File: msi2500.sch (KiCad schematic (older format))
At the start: 12 parts

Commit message: msi2500 full pcb design
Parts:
- removed U?: msi2500, symbol msi2500
- added C43: 10uF, symbol C
- added J10: GPIO2, Connectors:Pin_d0.7mm_L6.5mm_W1.8mm_FlatFork, symbol Conn_01x01
- added J11: GPIO3, Connectors:Pin_d0.7mm_L6.5mm_W1.8mm_FlatFork, symbol Conn_01x01
- added J7: VCC_GPIO, Connectors:Pin_d0.7mm_L6.5mm_W1.8mm_FlatFork, symbol Conn_01x01
- added J8: GPIO0, Connectors:Pin_d0.7mm_L6.5mm_W1.8mm_FlatFork, symbol Conn_01x01
- added J9: GPIO1, Connectors:Pin_d0.7mm_L6.5mm_W1.8mm_FlatFork, symbol Conn_01x01
- added U1: msi2500, Housings_DFN_QFN:QFN-32-1EP_5x5mm_Pitch0.5mm, symbol msi2500
- C1: renamed from C?; footprint (none) -> Capacitors_SMD:C_0603
- C2, C3, C4, C5, C6, C7: renamed from C?; footprint (none) -> Capacitors_SMD:C_0805
- C8, C9: renamed from C?; value C -> 18pF; footprint (none) -> Capacitors_SMD:C_0603
- R1: renamed from R?; footprint (none) -> Resistors_SMD:R_0603
- Y1: renamed from Y?; footprint (none) -> Crystals:Crystal_HC50_Vertical
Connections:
- net GND: now also C43.2, U1.17 (V15_VCO), U1.28 (XTAL_SEL), U1.29 (TEST1), U1.30 (TEST2), U1.33 (GND), U1.8 (VEE_ADC); no longer C3.1, C5.1
- net I_IN_N: now also U1.10 (IIN_N)
- net I_IN_P: now also U1.9 (IIN_P)
- net Q_IN_N: now also U1.12 (QIN_N)
- net Q_IN_P: now also U1.11 (QIN_P)
- net REFCLK: now also U1.24 (REFOUT)
- net SPI_CLK: now also U1.27 (SPI_CLK)
- net SPI_DATA: now also U1.26 (SPI_DAT)
- net SPI_LAT: now also U1.25 (SPI_LAT)
- net USB-DM: now also U1.20 (DM)
- net USB-DP: now also U1.19 (DP)
- net V18-SYNTH: now also U1.15 (V18_SYNTH)
- net VDDI: now also U1.31 (V18_DIGITAL)
- net at C4.1: now also U1.13 (V18_ADC)
- net at C7.1: now also U1.16 (V18_PHY)
- net at R1.2: now also U1.21 (REST)
- net at C9.2, Y1.2: now also U1.22 (X0)
- net at C8.2, Y1.1: now also U1.23 (X1)
- net at C1.1: now also U1.6 (ADC_REF_P)
- net at C1.2: now also U1.7 (ADC_REF_N)
- new net: J7.1 (Pin_1), U1.1 (VCC_GPIO)
- new net: J8.1 (Pin_1), U1.2 (GPIO_0)
- new net: J9.1 (Pin_1), U1.3 (GPIO_1)
- new net: J10.1 (Pin_1), U1.4 (GPIO_2)
- new net: J11.1 (Pin_1), U1.5 (GPIO_3)
- new net VDIG: C3.1, C43.1, C5.1, U1.14 (VCC_3V_PM), U1.18 (VCC_3V_XCVR), U1.32 (VCC_3V_DIGITAL)
- no-connect marks 5 -> 0

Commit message: update and fix bug
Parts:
- C7: renamed from C43; footprint (none) -> Capacitors_SMD:C_0805
- renumbered C9 to C10, C7 to C8, C8 to C9, J7 to J1, J8 to J2, J9 to J3, J10 to J4, J11 to J5
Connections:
- net USB-DM renamed USB_DM
- net USB-DP renamed USB_DP
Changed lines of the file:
@@
 	5100 4800 5100 4600
 Wire Wire Line
-	5200 4600 5200 4950
-Wire Wire Line
 	5200 4950 3700 4950
 Wire Wire Line
@@
 Wire Wire Line
 	5300 5100 5300 4600
-Wire Wire Line
-	5400 4600 5400 5250
 Wire Wire Line
 	5400 5250 3700 5250
@@
 	4550 4250 4550 4450
 $Comp
-L C C7
+L C C8
 U 1 1 5C68D5CF
 P 6950 5450
-F 0 "C7" H 6975 5550 50  0000 L CNN
+F 0 "C8" H 6975 5550 50  0000 L CNN
 F 1 "1uF" H 6975 5350 50  0000 L CNN
 F 2 "Capacitors_SMD:C_0805" H 6988 5300 50  0001 C CNN
@@
 Wire Wire Line
 	5700 5600 5900 5600
-Text GLabel 5900 5600 2    39   Output ~ 0
+Text GLabel 5900 5600 2    39   Input ~ 0
 V18-SYNTH
 Wire Wire Line
@@
 	6450 4250 6450 4500
 Connection ~ 6800 4150
-Text GLabel 7000 3950 2    39   BiDi ~ 0
-USB-DM
+Text GLabel 7000 3950 2    39   Input ~ 0
+USB_DM
 Wire Wire Line
 	6250 4050 7000 4050
-Text GLabel 7000 4050 2    39   BiDi ~ 0
-USB-DP
+Text GLabel 7000 4050 2    39   Input ~ 0
+USB_DP
 Wire Wire Line
 	6250 3950 7000 3950
@@
 Wire Wire Line
 	7050 3800 7300 3800
-Text GLabel 6700 3100 2    39   Output ~ 0
+Text GLabel 6700 3100 2    39   Input ~ 0
 REFCLK
-Wire Wire Line
-	6250 3550 6300 3550
-Wire Wire Line
-	6300 3550 6300 3100
 Wire Wire Line
 	6300 3100 6700 3100
@@
 $EndComp
 $Comp
-L C C8
+L C C9
 U 1 1 5C68E41D
 P 7500 3200
-F 0 "C8" H 7525 3300 50  0000 L CNN
+F 0 "C9" H 7525 3300 50  0000 L CNN
 F 1 "18pF" H 7300 3100 50  0000 L CNN
 F 2 "Capacitors_SMD:C_0603" H 7538 3050 50  0001 C CNN
@@
 $EndComp
 $Comp
-L C C9
+L C C10
 U 1 1 5C68E476
 P 7500 3600
-F 0 "C9" H 7525 3700 50  0000 L CNN
+F 0 "C10" H 7525 3700 50  0000 L CNN
 F 1 "18pF" H 7300 3500 50  0000 L CNN
 F 2 "Capacitors_SMD:C_0603" H 7538 3450 50  0001 C CNN
@@
 	4900 2350 5150 2350
 Connection ~ 5150 2800
-Text GLabel 5350 1950 2    39   Output ~ 0
+Text GLabel 5350 1950 2    39   Input ~ 0
 VDDI
 Wire Wire Line
@@
 Wire Wire Line
 	4600 2050 4450 2050
-Text GLabel 5650 2350 1    39   Output ~ 0
+Text GLabel 5650 2350 1    39   Input ~ 0
 SPI_CLK
-Text GLabel 5750 2350 1    39   BiDi ~ 0
+Text GLabel 5750 2350 1    39   Input ~ 0
 SPI_DATA
-Text GLabel 5850 2350 1    39   Output ~ 0
+Text GLabel 5850 2350 1    39   Input ~ 0
 SPI_LAT
 Wire Wire Line
-	5650 3200 5650 2350
-Wire Wire Line
 	5750 2350 5750 3200
-Wire Wire Line
-	5850 3200 5850 2350
-$Comp
-L C C43
+$Comp
+L C C7
 U 1 1 5C6965F5
 P 6800 4400
-F 0 "C43" H 6825 4500 50  0000 L CNN
+F 0 "C7" H 6825 4500 50  0000 L CNN
 F 1 "10uF" H 6825 4300 50  0000 L CNN
-F 2 "" H 6838 4250 50  0001 C CNN
+F 2 "Capacitors_SMD:C_0805" H 6838 4250 50  0001 C CNN
 F 3 "" H 6800 4400 50  0001 C CNN
 	1    6800 4400
@@
 $EndComp
 $Comp
-L Conn_01x01 J7
+L Conn_01x01 J1
 U 1 1 5C69B0A4
 P 3500 3000
-F 0 "J7" H 3500 3100 50  0000 C CNN
+F 0 "J1" H 3500 3100 50  0000 C CNN
 F 1 "VCC_GPIO" H 3500 2900 50  0000 C CNN
 F 2 "Connectors:Pin_d0.7mm_L6.5mm_W1.8mm_FlatFork" H 3500 3000 50  0001 C CNN
@@
 $EndComp
 $Comp
-L Conn_01x01 J8
+L Conn_01x01 J2
 U 1 1 5C69B155
 P 3500 3300
-F 0 "J8" H 3500 3400 50  0000 C CNN
+F 0 "J2" H 3500 3400 50  0000 C CNN
 F 1 "GPIO0" H 3500 3200 50  0000 C CNN
 F 2 "Connectors:Pin_d0.7mm_L6.5mm_W1.8mm_FlatFork" H 3500 3300 50  0001 C CNN
@@
 $EndComp
 $Comp
-L Conn_01x01 J9
+L Conn_01x01 J3
 U 1 1 5C69B1C1
 P 3500 3600
-F 0 "J9" H 3500 3700 50  0000 C CNN
+F 0 "J3" H 3500 3700 50  0000 C CNN
 F 1 "GPIO1" H 3500 3500 50  0000 C CNN
 F 2 "Connectors:Pin_d0.7mm_L6.5mm_W1.8mm_FlatFork" H 3500 3600 50  0001 C CNN
@@
 $EndComp
 $Comp
-L Conn_01x01 J10
+L Conn_01x01 J4
 U 1 1 5C69B1C7
 P 3500 3900
-F 0 "J10" H 3500 4000 50  0000 C CNN
+F 0 "J4" H 3500 4000 50  0000 C CNN
 F 1 "GPIO2" H 3500 3800 50  0000 C CNN
 F 2 "Connectors:Pin_d0.7mm_L6.5mm_W1.8mm_FlatFork" H 3500 3900 50  0001 C CNN
@@
 $EndComp
 $Comp
-L Conn_01x01 J11
+L Conn_01x01 J5
 U 1 1 5C69B2AD
 P 3500 4200
-F 0 "J11" H 3500 4300 50  0000 C CNN
+F 0 "J5" H 3500 4300 50  0000 C CNN
 F 1 "GPIO3" H 3500 4100 50  0000 C CNN
 F 2 "Connectors:Pin_d0.7mm_L6.5mm_W1.8mm_FlatFork" H 3500 4200 50  0001 C CNN
@@
 Wire Wire Line
 	3900 4200 3700 4200
+Wire Wire Line
+	5200 4600 5200 4950
+Wire Wire Line
+	5400 5250 5400 4600
+Wire Wire Line
+	6300 3100 6300 3550
+Wire Wire Line
+	6300 3550 6250 3550
+Wire Wire Line
+	5650 3200 5650 2350
+Wire Wire Line
+	5850 3200 5850 2350
 $EndSCHEMATC

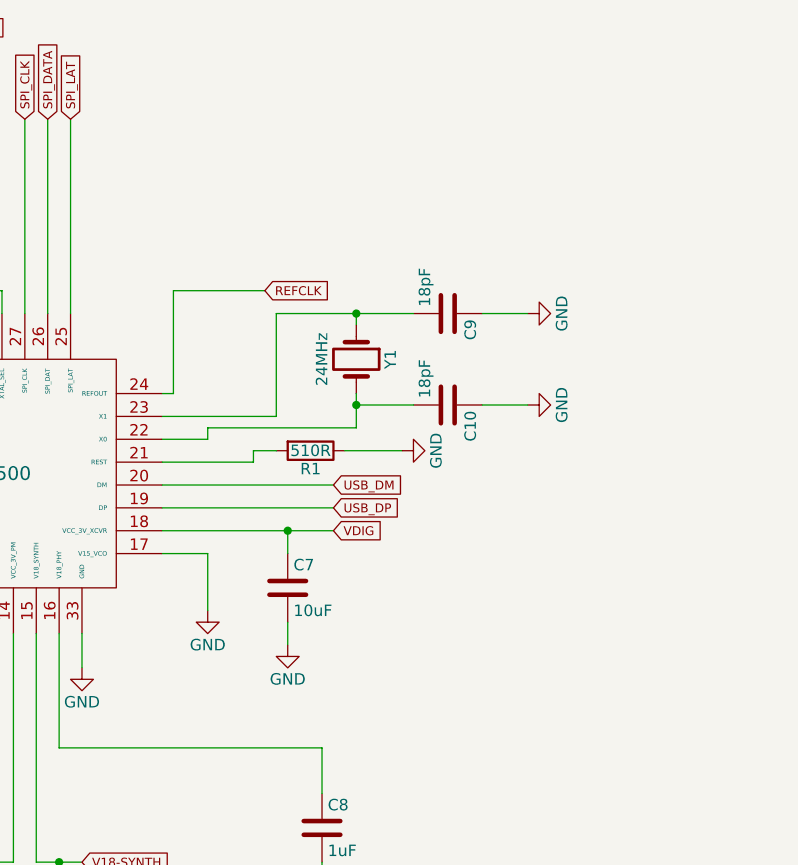
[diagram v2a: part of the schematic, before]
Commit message: use external oscillator repace xtal and add a led
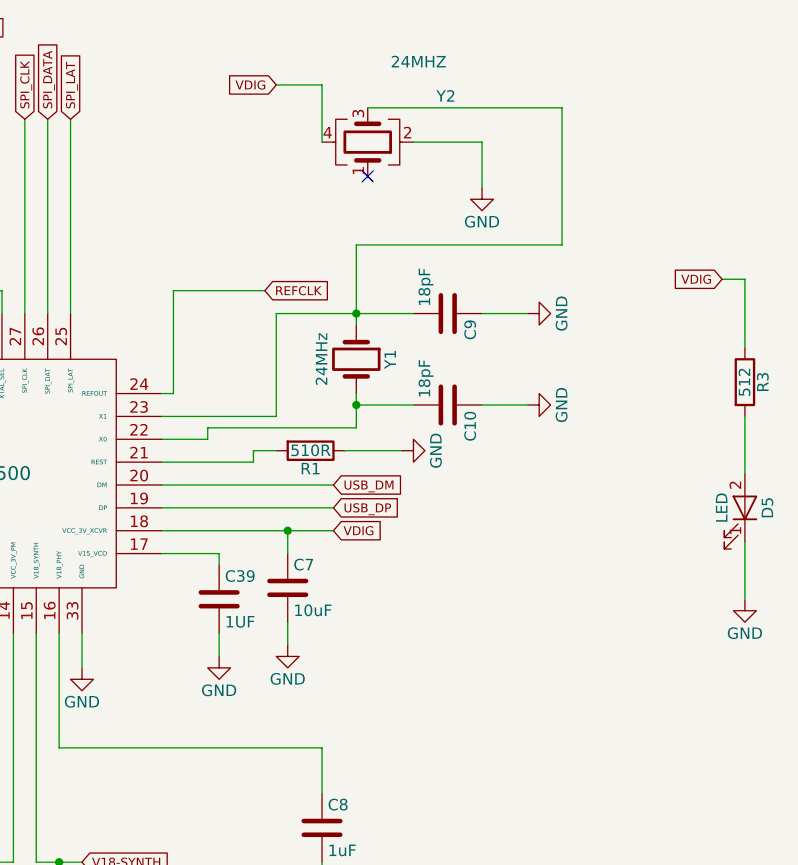
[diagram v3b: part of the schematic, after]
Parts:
- added C39: 1UF, Capacitors_SMD:C_0805, symbol C
- added D5: LED, Diodes_THT:D_DO-35_SOD27_P2.54mm_Vertical_AnodeUp, symbol LED
- added R3: 512, Resistors_SMD:R_0603, symbol R
- added Y2: 24MHZ, Crystals:Crystal_SMD_0603-4pin_6.0x3.5mm_HandSoldering, symbol Crystal_GND24
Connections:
- net GND: now also C39.2, D5.1 (K), Y2.2; no longer U1.17 (V15_VCO)
- net VDIG: now also R3.1, Y2.4
- net at C9.2, U1.23 (X1), Y1.1: now also Y2.3
- new net: C39.1, U1.17 (V15_VCO)
- new net: D5.2 (A), R3.2
- no-connect marks 0 -> 1
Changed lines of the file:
@@
 L GND #PWR9
 U 1 1 5C68DD59
-P 6450 4500
-F 0 "#PWR9" H 6450 4250 50  0001 C CNN
-F 1 "GND" H 6450 4350 50  0000 C CNN
-F 2 "" H 6450 4500 50  0001 C CNN
-F 3 "" H 6450 4500 50  0001 C CNN
-	1    6450 4500
+P 6500 4700
+F 0 "#PWR9" H 6500 4450 50  0001 C CNN
+F 1 "GND" H 6500 4550 50  0000 C CNN
+F 2 "" H 6500 4700 50  0001 C CNN
+F 3 "" H 6500 4700 50  0001 C CNN
+	1    6500 4700
 	1    0    0    -1
 $EndComp
@@
 	6250 4150 7000 4150
 Wire Wire Line
-	6250 4250 6450 4250
-Wire Wire Line
-	6450 4250 6450 4500
+	6250 4250 6500 4250
 Connection ~ 6800 4150
 Text GLabel 7000 3950 2    39   Input ~ 0
@@
 $EndComp
 $Comp
-L GND #PWR13
+L GND #PWR14
 U 1 1 5C68E538
 P 7850 3200
-F 0 "#PWR13" H 7850 2950 50  0001 C CNN
+F 0 "#PWR14" H 7850 2950 50  0001 C CNN
 F 1 "GND" H 7850 3050 50  0000 C CNN
 F 2 "" H 7850 3200 50  0001 C CNN
@@
 $EndComp
 $Comp
-L GND #PWR14
+L GND #PWR15
 U 1 1 5C68E5AE
 P 7850 3600
-F 0 "#PWR14" H 7850 3350 50  0001 C CNN
+F 0 "#PWR15" H 7850 3350 50  0001 C CNN
 F 1 "GND" H 7850 3450 50  0000 C CNN
 F 2 "" H 7850 3600 50  0001 C CNN
@@
 	6750 3200 7350 3200
 Wire Wire Line
-	7100 3200 7100 3250
+	7100 2900 7100 3250
 Wire Wire Line
 	7350 3600 7100 3600
@@
 Wire Wire Line
 	5850 3200 5850 2350
+$Comp
+L C C39
+U 1 1 5C79333B
+P 6500 4450
+F 0 "C39" H 6525 4550 50  0000 L CNN
+F 1 "1UF" H 6525 4350 50  0000 L CNN
+F 2 "Capacitors_SMD:C_0805" H 6538 4300 50  0001 C CNN
+F 3 "" H 6500 4450 50  0001 C CNN
+	1    6500 4450
+	1    0    0    -1
+$EndComp
+Wire Wire Line
+	6500 4250 6500 4300
+Wire Wire Line
+	6500 4600 6500 4700
+$Comp
+L Crystal_GND24 Y2
+U 1 1 5CA9F9E8
+P 7150 2450
+F 0 "Y2" V 7350 2750 50  0000 L CNN
+F 1 "24MHZ" V 7500 2550 50  0000 L CNN
+F 2 "Crystals:Crystal_SMD_0603-4pin_6.0x3.5mm_HandSoldering" H 7150 2450 50  0001 C CNN
+F 3 "" H 7150 2450 50  0001 C CNN
+	1    7150 2450
+	0    1    -1   0
+$EndComp
+Text GLabel 6750 2200 0    39   Input ~ 0
+VDIG
+Wire Wire Line
+	6950 2450 6950 2200
+Wire Wire Line
+	6950 2200 6750 2200
+$Comp
+L GND #PWR13
+U 1 1 5CAA05D3
+P 7650 2650
+F 0 "#PWR13" H 7650 2400 50  0001 C CNN
+F 1 "GND" H 7650 2500 50  0000 C CNN
+F 2 "" H 7650 2650 50  0001 C CNN
+F 3 "" H 7650 2650 50  0001 C CNN
+	1    7650 2650
+	1    0    0    -1
+$EndComp
+Wire Wire Line
+	7350 2450 7650 2450
+Wire Wire Line
+	7650 2450 7650 2650
+Wire Wire Line
+	7150 2300 8000 2300
+Wire Wire Line
+	8000 2300 8000 2900
+Wire Wire Line
+	8000 2900 7100 2900
+NoConn ~ 7150 2600
+$Comp
+L LED D5
+U 1 1 5CAA11F1
+P 8800 4050
+F 0 "D5" H 8800 4150 50  0000 C CNN
+F 1 "LED" H 8800 3950 50  0000 C CNN
+F 2 "Diodes_THT:D_DO-35_SOD27_P2.54mm_Vertical_AnodeUp" H 8800 4050 50  0001 C CNN
+F 3 "" H 8800 4050 50  0001 C CNN
+	1    8800 4050
+	0    1    -1   0
+$EndComp
+$Comp
+L R R3
+U 1 1 5CAA13AD
+P 8800 3500
+F 0 "R3" V 8880 3500 50  0000 C CNN
+F 1 "512" V 8800 3500 50  0000 C CNN
+F 2 "Resistors_SMD:R_0603" V 8730 3500 50  0001 C CNN
+F 3 "" H 8800 3500 50  0001 C CNN
+	1    8800 3500
+	1    0    0    -1
+$EndComp
+Wire Wire Line
+	8800 3650 8800 3900
+$Comp
+L GND #PWR16
+U 1 1 5CAA16D2
+P 8800 4450
+F 0 "#PWR16" H 8800 4200 50  0001 C CNN
+F 1 "GND" H 8800 4300 50  0000 C CNN
+F 2 "" H 8800 4450 50  0001 C CNN
+F 3 "" H 8800 4450 50  0001 C CNN
+	1    8800 4450
+	1    0    0    -1
+$EndComp
+Wire Wire Line
+	8800 4450 8800 4200
+Text GLabel 8700 3050 0    39   Input ~ 0
+VDIG
+Wire Wire Line
+	8800 3350 8800 3050
+Wire Wire Line
+	8800 3050 8700 3050
 $EndSCHEMATC

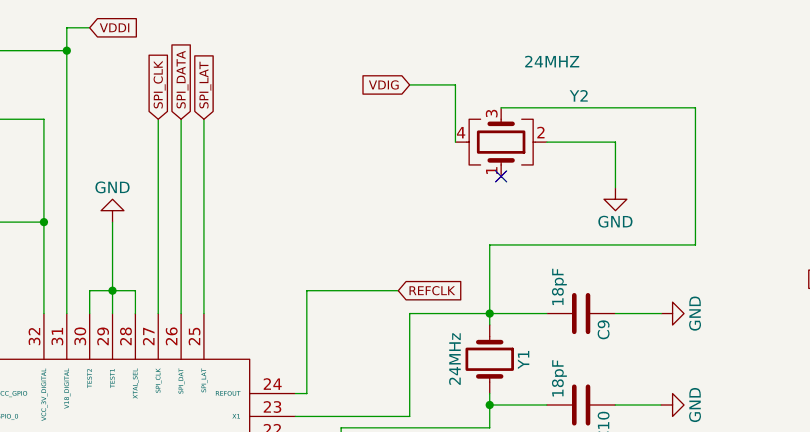
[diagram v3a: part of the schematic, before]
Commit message: replace ldo and finish osc pcb layout
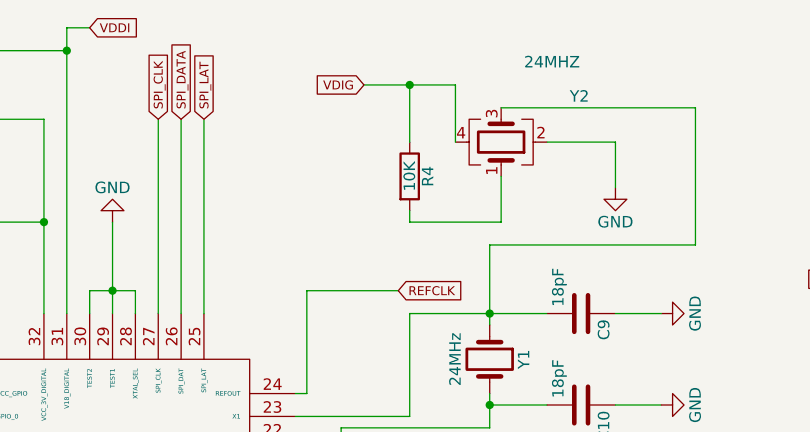
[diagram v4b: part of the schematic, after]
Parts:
- added R4: 10K, Resistors_SMD:R_0603, symbol R
- Y2: footprint Crystals:Crystal_SMD_0603-4pin_6.0x3.5mm_HandSoldering -> Crystals:Crystal_SMD_7050-4pin_7.0x5.0mm
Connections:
- net VDIG: now also R4.1
- net at Y2.1: now also R4.2
- no-connect marks 1 -> 0
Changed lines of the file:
@@
 $EndDescr
 $Comp
-L GND #PWR5
+L GND #PWR01
 U 1 1 5C68D20C
 P 5450 2800
-F 0 "#PWR5" H 5450 2550 50  0001 C CNN
+F 0 "#PWR01" H 5450 2550 50  0001 C CNN
 F 1 "GND" H 5450 2650 50  0000 C CNN
 F 2 "" H 5450 2800 50  0001 C CNN
@@
 $EndComp
 $Comp
-L GND #PWR8
+L GND #PWR02
 U 1 1 5C68D2D4
 P 5900 4750
-F 0 "#PWR8" H 5900 4500 50  0001 C CNN
+F 0 "#PWR02" H 5900 4500 50  0001 C CNN
 F 1 "GND" H 5900 4600 50  0000 C CNN
 F 2 "" H 5900 4750 50  0001 C CNN
@@
 	4350 3950 4050 3950
 $Comp
-L GND #PWR3
+L GND #PWR03
 U 1 1 5C68D520
 P 4550 4450
-F 0 "#PWR3" H 4550 4200 50  0001 C CNN
+F 0 "#PWR03" H 4550 4200 50  0001 C CNN
 F 1 "GND" H 4550 4300 50  0000 C CNN
 F 2 "" H 4550 4450 50  0001 C CNN
@@
 	5800 5100 6950 5100
 $Comp
-L GND #PWR4
+L GND #PWR04
 U 1 1 5C68D665
 P 4850 5850
-F 0 "#PWR4" H 4850 5600 50  0001 C CNN
+F 0 "#PWR04" H 4850 5600 50  0001 C CNN
 F 1 "GND" H 4850 5700 50  0000 C CNN
 F 2 "" H 4850 5850 50  0001 C CNN
@@
 $EndComp
 $Comp
-L GND #PWR11
+L GND #PWR05
 U 1 1 5C68D681
 P 6950 5800
-F 0 "#PWR11" H 6950 5550 50  0001 C CNN
+F 0 "#PWR05" H 6950 5550 50  0001 C CNN
 F 1 "GND" H 6950 5650 50  0000 C CNN
 F 2 "" H 6950 5800 50  0001 C CNN
@@
 Connection ~ 5800 5600
 $Comp
-L GND #PWR6
+L GND #PWR06
 U 1 1 5C68DAB6
 P 5500 6150
-F 0 "#PWR6" H 5500 5900 50  0001 C CNN
+F 0 "#PWR06" H 5500 5900 50  0001 C CNN
 F 1 "GND" H 5500 6000 50  0000 C CNN
 F 2 "" H 5500 6150 50  0001 C CNN
@@
 $EndComp
 $Comp
-L GND #PWR7
+L GND #PWR07
 U 1 1 5C68DAD6
 P 5800 6150
-F 0 "#PWR7" H 5800 5900 50  0001 C CNN
+F 0 "#PWR07" H 5800 5900 50  0001 C CNN
 F 1 "GND" H 5800 6000 50  0000 C CNN
 F 2 "" H 5800 6150 50  0001 C CNN
@@
 VDIG
 $Comp
-L GND #PWR9
+L GND #PWR08
 U 1 1 5C68DD59
 P 6500 4700
-F 0 "#PWR9" H 6500 4450 50  0001 C CNN
+F 0 "#PWR08" H 6500 4450 50  0001 C CNN
 F 1 "GND" H 6500 4550 50  0000 C CNN
 F 2 "" H 6500 4700 50  0001 C CNN
@@
 $EndComp
 $Comp
-L GND #PWR10
+L GND #PWR09
 U 1 1 5C68DD79
 P 6800 4650
-F 0 "#PWR10" H 6800 4400 50  0001 C CNN
+F 0 "#PWR09" H 6800 4400 50  0001 C CNN
 F 1 "GND" H 6800 4500 50  0000 C CNN
 F 2 "" H 6800 4650 50  0001 C CNN
@@
 	6250 3950 7000 3950
 $Comp
-L GND #PWR12
+L GND #PWR010
 U 1 1 5C68E182
 P 7300 3800
-F 0 "#PWR12" H 7300 3550 50  0001 C CNN
+F 0 "#PWR010" H 7300 3550 50  0001 C CNN
 F 1 "GND" H 7300 3650 50  0000 C CNN
 F 2 "" H 7300 3800 50  0001 C CNN
@@
 $EndComp
 $Comp
-L GND #PWR14
+L GND #PWR011
 U 1 1 5C68E538
 P 7850 3200
-F 0 "#PWR14" H 7850 2950 50  0001 C CNN
+F 0 "#PWR011" H 7850 2950 50  0001 C CNN
 F 1 "GND" H 7850 3050 50  0000 C CNN
 F 2 "" H 7850 3200 50  0001 C CNN
@@
 $EndComp
 $Comp
-L GND #PWR15
+L GND #PWR012
 U 1 1 5C68E5AE
 P 7850 3600
-F 0 "#PWR15" H 7850 3350 50  0001 C CNN
+F 0 "#PWR012" H 7850 3350 50  0001 C CNN
 F 1 "GND" H 7850 3450 50  0000 C CNN
 F 2 "" H 7850 3600 50  0001 C CNN
@@
 Connection ~ 7100 3600
 $Comp
-L GND #PWR2
+L GND #PWR013
 U 1 1 5C68EA62
 P 4450 2800
-F 0 "#PWR2" H 4450 2550 50  0001 C CNN
+F 0 "#PWR013" H 4450 2550 50  0001 C CNN
 F 1 "GND" H 4450 2650 50  0000 C CNN
 F 2 "" H 4450 2800 50  0001 C CNN
@@
 $EndComp
 $Comp
-L GND #PWR1
+L GND #PWR014
 U 1 1 5C68F152
 P 4450 2050
-F 0 "#PWR1" H 4450 1800 50  0001 C CNN
+F 0 "#PWR014" H 4450 1800 50  0001 C CNN
 F 1 "GND" H 4450 1900 50  0000 C CNN
 F 2 "" H 4450 2050 50  0001 C CNN
@@
 F 0 "Y2" V 7350 2750 50  0000 L CNN
 F 1 "24MHZ" V 7500 2550 50  0000 L CNN
-F 2 "Crystals:Crystal_SMD_0603-4pin_6.0x3.5mm_HandSoldering" H 7150 2450 50  0001 C CNN
+F 2 "Crystals:Crystal_SMD_7050-4pin_7.0x5.0mm" H 7150 2450 50  0001 C CNN
 F 3 "" H 7150 2450 50  0001 C CNN
 	1    7150 2450
 	0    1    -1   0
 $EndComp
-Text GLabel 6750 2200 0    39   Input ~ 0
+Text GLabel 6550 2200 0    39   Input ~ 0
 VDIG
 Wire Wire Line
-	6950 2450 6950 2200
-Wire Wire Line
-	6950 2200 6750 2200
-$Comp
-L GND #PWR13
+	6950 2200 6950 2450
+Wire Wire Line
+	6550 2200 6950 2200
+$Comp
+L GND #PWR015
 U 1 1 5CAA05D3
 P 7650 2650
-F 0 "#PWR13" H 7650 2400 50  0001 C CNN
+F 0 "#PWR015" H 7650 2400 50  0001 C CNN
 F 1 "GND" H 7650 2500 50  0000 C CNN
 F 2 "" H 7650 2650 50  0001 C CNN
@@
 Wire Wire Line
 	8000 2900 7100 2900
-NoConn ~ 7150 2600
 $Comp
 L LED D5
@@
 	8800 3650 8800 3900
 $Comp
-L GND #PWR16
+L GND #PWR016
 U 1 1 5CAA16D2
 P 8800 4450
-F 0 "#PWR16" H 8800 4200 50  0001 C CNN
+F 0 "#PWR016" H 8800 4200 50  0001 C CNN
 F 1 "GND" H 8800 4300 50  0000 C CNN
 F 2 "" H 8800 4450 50  0001 C CNN
@@
 Wire Wire Line
 	8800 3050 8700 3050
+$Comp
+L R R4
+U 1 1 5CB19DE2
+P 6750 2600
+F 0 "R4" V 6830 2600 50  0000 C CNN
+F 1 "10K" V 6750 2600 50  0000 C CNN
+F 2 "Resistors_SMD:R_0603" V 6680 2600 50  0001 C CNN
+F 3 "" H 6750 2600 50  0001 C CNN
+	1    6750 2600
+	1    0    0    -1
+$EndComp
+Wire Wire Line
+	7150 2600 7150 2800
+Wire Wire Line
+	7150 2800 6750 2800
+Wire Wire Line
+	6750 2800 6750 2750
+Wire Wire Line
+	6750 2450 6750 2200
+Connection ~ 6750 2200
 $EndSCHEMATC

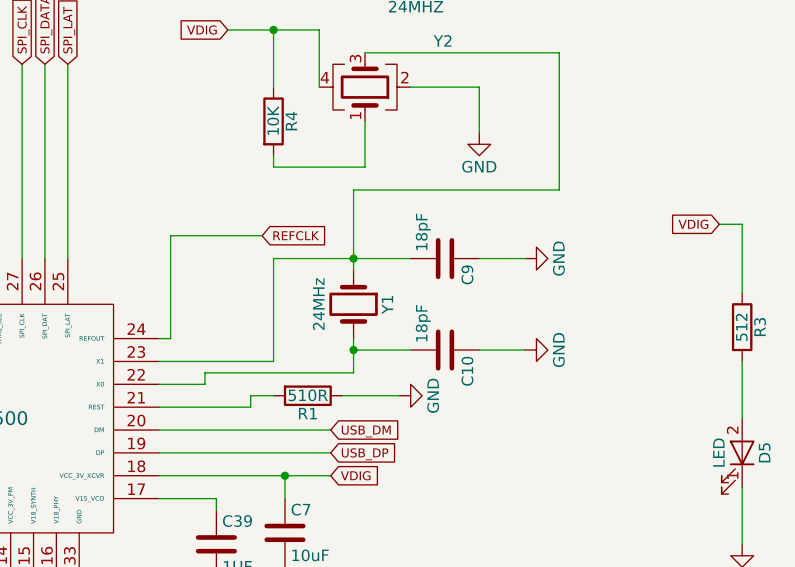
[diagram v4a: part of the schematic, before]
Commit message: fix oscillator connect to x1 error
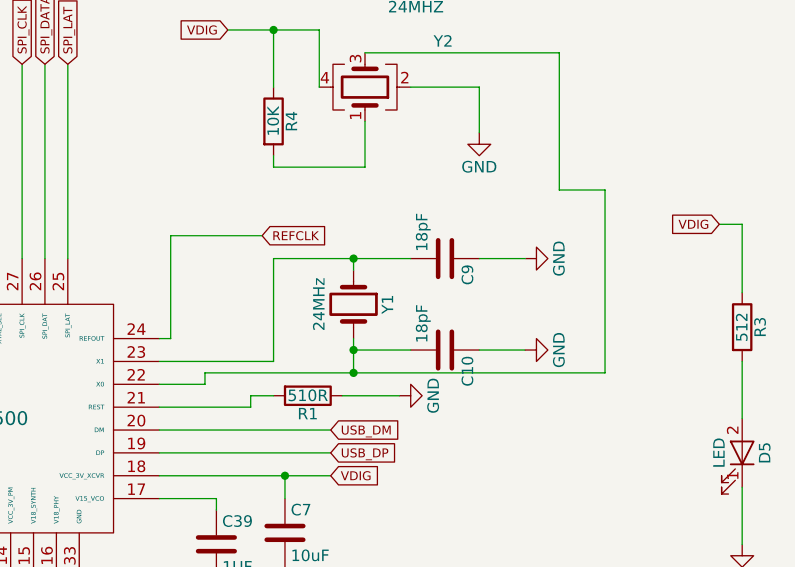
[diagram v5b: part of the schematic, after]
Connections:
- net at C9.2, U1.23 (X1), Y1.1: no longer Y2.3
- net at C10.2, U1.22 (X0), Y1.2: now also Y2.3
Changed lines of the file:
@@
 	6750 3200 7350 3200
-Wire Wire Line
-	7100 2900 7100 3250
 Wire Wire Line
 	7350 3600 7100 3600
@@
 	6450 3750 6450 3700
 Wire Wire Line
-	6450 3700 7100 3700
+	6450 3700 8200 3700
 Connection ~ 7100 3600
 $Comp
@@
 Wire Wire Line
 	8000 2300 8000 2900
-Wire Wire Line
-	8000 2900 7100 2900
 $Comp
 L LED D5
@@
 	6750 2450 6750 2200
 Connection ~ 6750 2200
+Wire Wire Line
+	8000 2900 8200 2900
+Wire Wire Line
+	8200 2900 8200 3700
+Connection ~ 7100 3700
+Wire Wire Line
+	7100 3250 7100 3200
 $EndSCHEMATC
